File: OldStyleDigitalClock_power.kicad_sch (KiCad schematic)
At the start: 22 parts, among them J1 USB_C_IN, J2 USB_A_OUT, J3 USB_A_OUT, U14 NA555P

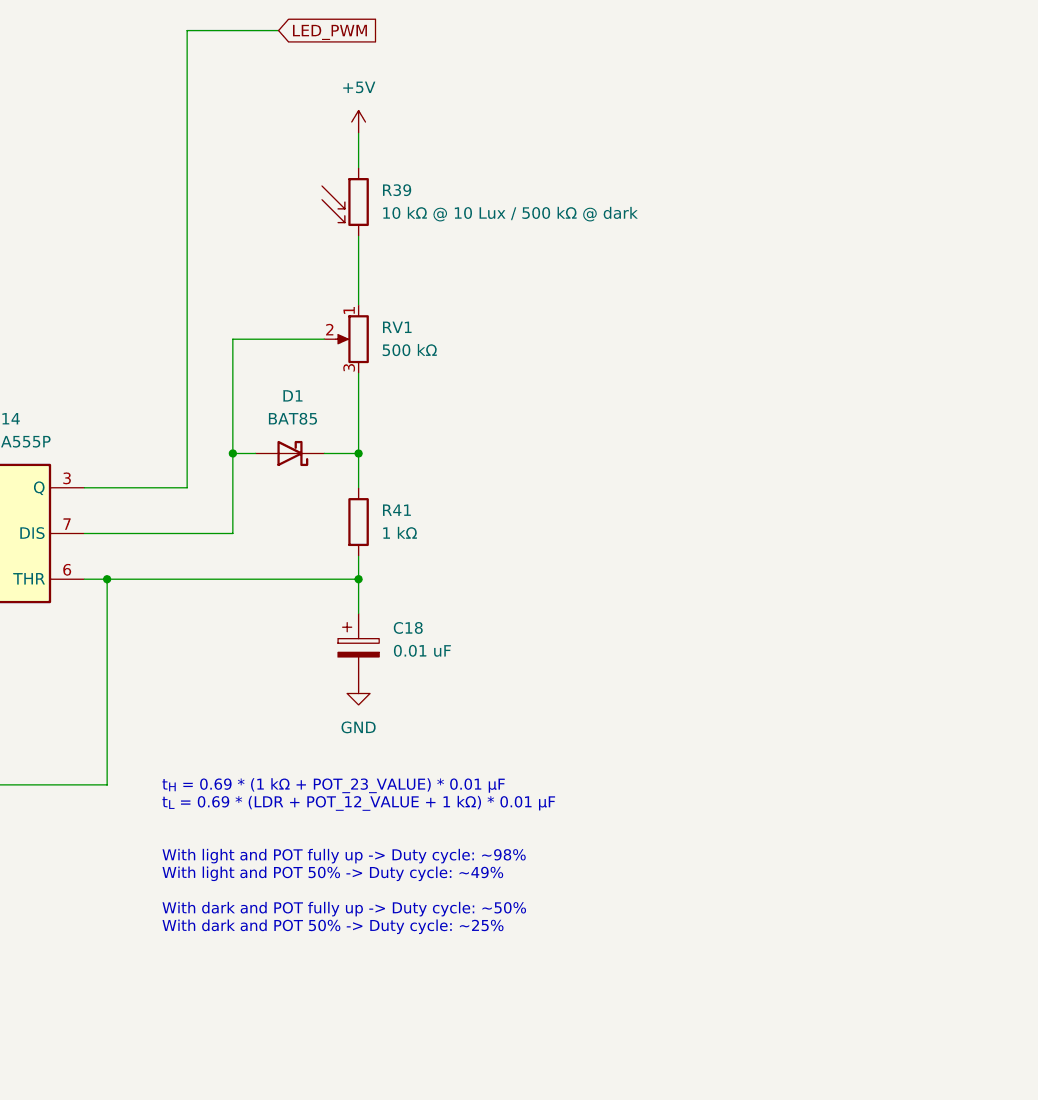
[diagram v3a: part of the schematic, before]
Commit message: Updated PWM calculations
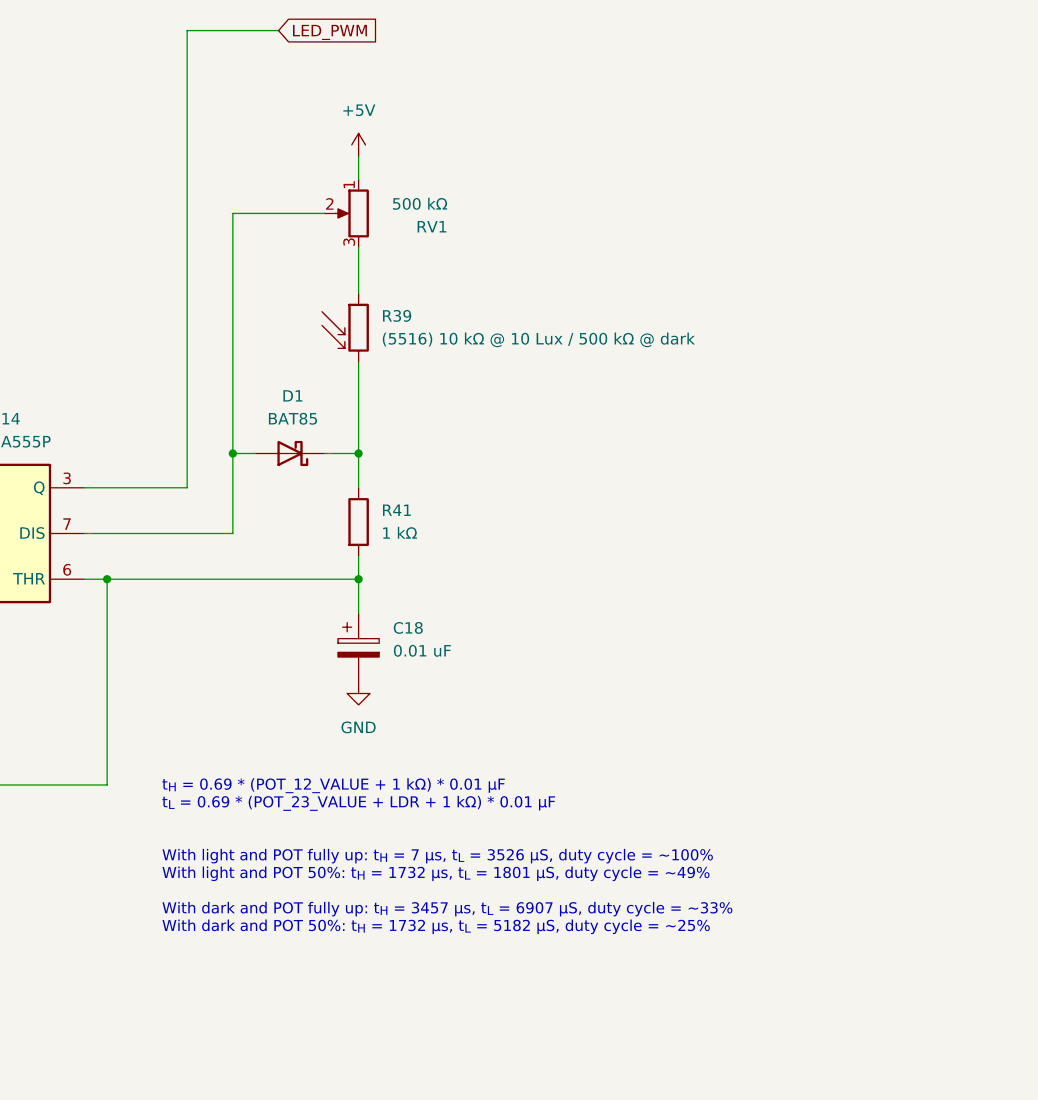
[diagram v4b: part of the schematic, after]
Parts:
- R39: value 10 kΩ @ 10 Lux / 500 kΩ @ dark -> (5516) 10 kΩ @ 10 Lux / 500 kΩ @ dark
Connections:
- net +5V: now also RV1.1; no longer R39.1
- net at R39.2: now also D1.1 (K), R41.1; no longer RV1.1
- new net: R39.1, RV1.3
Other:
- note added: "t_{H} = 0.69 * (POT_12_VALUE + 1 kΩ) * 0.01 µF t_{L} = 0.69 * (POT_23_VALUE + LDR + 1 kΩ) * 0.01 µF With light and POT fully up: t_{H} = 7 µs, t_{L} = 3526 µS, duty cycle = ~100% With light and POT 50%: t_{H} = 1732 µs, t_{L} = 1801 µS, duty cycle = ~49% With dark and POT fully up: t_{H} = 3457 µs, t_{L} = 6907 µS, duty cycle = ~33% With dark and POT 50%: t_{H} = 1732 µs, t_{L} = 5182 µS, duty cy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"
- note removed: "t_{H} = 0.69 * (1 kΩ + POT_23_VALUE) * 0.01 µF t_{L} = 0.69 * (LDR + POT_12_VALUE + 1 kΩ) * 0.01 µF With light and POT fully up -> Duty cycle: ~98% With light and POT 50% -> Duty cycle: ~49% With dark and POT fully up -> Duty cycle: ~50% With dark and POT 50% -> Duty cycle: ~25%"
- moved on the sheet: R39, RV1
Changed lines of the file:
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@@
 		(company "Pasquale Lafiosca")
 	)
-	(text "t_{H} = 0.69 * (1 kΩ + POT_23_VALUE) * 0.01 µF\nt_{L} = 0.69 * (LDR + POT_12_VALUE + 1 kΩ) * 0.01 µF\n\n\nWith light and POT fully up -> Duty cycle: ~98%\nWith light and POT 50% -> Duty cycle: ~49%\n\nWith dark and POT fully up -> Duty cycle: ~50%\nWith dark and POT 50% -> Duty cycle: ~25%"
+	(text "t_{H} = 0.69 * (POT_12_VALUE + 1 kΩ) * 0.01 µF\nt_{L} = 0.69 * (POT_23_VALUE + LDR + 1 kΩ) * 0.01 µF\n\n\nWith light and POT fully up: t_{H} = 7 µs, t_{L} = 3526 µS, duty cycle = ~100%\nWith light and POT 50%: t_{H} = 1732 µs, t_{L} = 1801 µS, duty cycle = ~49%\n\nWith dark and POT fully up: t_{H} = 3457 µs, t_{L} = 6907 µS, duty cycle = ~33%\nWith dark and POT 50%: t_{H} = 1732 µs, t_{L} = 5182 µS, duty cycle = ~25%"
 		(exclude_from_sim no)
 		(at 211.836 111.252 0)
@@
 	)
 	(junction
+		(at 233.68 74.93)
+		(diameter 0)
+		(color 0 0 0 0)
+	)
+	(junction
 		(at 38.1 185.42)
 		(diameter 0)
@@
 	)
 	(junction
-		(at 233.68 74.93)
-		(diameter 0)
-		(color 0 0 0 0)
-	)
-	(junction
 		(at 167.64 67.31)
 		(diameter 0)
@@
 	(wire
 		(pts
+			(xy 219.71 48.26) (xy 219.71 74.93)
+		)
+		(stroke
+			(width 0)
+			(type default)
+		)
+	)
+	(wire
+		(pts
 			(xy 40.64 35.56) (xy 41.91 35.56)
 		)
@@
 	(wire
 		(pts
-			(xy 233.68 39.37) (xy 233.68 43.18)
-		)
-		(stroke
-			(width 0)
-			(type default)
-		)
-	)
-	(wire
-		(pts
 			(xy 88.9 69.85) (xy 88.9 80.01)
 		)
@@
 	(wire
 		(pts
+			(xy 233.68 64.77) (xy 233.68 74.93)
+		)
+		(stroke
+			(width 0)
+			(type default)
+		)
+	)
+	(wire
+		(pts
 			(xy 133.35 90.17) (xy 124.46 90.17)
 		)
@@
 	(wire
 		(pts
-			(xy 219.71 62.23) (xy 229.87 62.23)
-		)
-		(stroke
-			(width 0)
-			(type default)
-		)
-	)
-	(wire
-		(pts
 			(xy 68.58 109.22) (xy 78.74 109.22)
 		)
@@
 	(wire
 		(pts
+			(xy 233.68 41.91) (xy 233.68 44.45)
+		)
+		(stroke
+			(width 0)
+			(type default)
+		)
+	)
+	(wire
+		(pts
 			(xy 68.58 109.22) (xy 68.58 110.49)
 		)
@@
 	(wire
 		(pts
-			(xy 219.71 62.23) (xy 219.71 74.93)
-		)
-		(stroke
-			(width 0)
-			(type default)
-		)
-	)
-	(wire
-		(pts
 			(xy 54.61 69.85) (xy 71.12 69.85)
 		)
@@
 	(wire
 		(pts
-			(xy 233.68 66.04) (xy 233.68 74.93)
+			(xy 233.68 52.07) (xy 233.68 57.15)
 		)
 		(stroke
@@
 	(wire
 		(pts
-			(xy 233.68 50.8) (xy 233.68 58.42)
-		)
-		(stroke
-			(width 0)
-			(type default)
-		)
-	)
-	(wire
-		(pts
 			(xy 31.75 107.95) (xy 31.75 109.22)
 		)
@@
 		(pts
 			(xy 233.68 88.9) (xy 233.68 86.36)
+		)
+		(stroke
+			(width 0)
+			(type default)
+		)
+	)
+	(wire
+		(pts
+			(xy 219.71 48.26) (xy 229.87 48.26)
 		)
 		(stroke
@@
 	(symbol
 		(lib_id "Device:R_Potentiometer")
-		(at 233.68 62.23 0)
+		(at 233.68 48.26 0)
 		(mirror y)
 		(unit 1)
@@
 		(dnp no)
 		(property "Reference" "RV1"
-			(at 236.22 60.9599 0)
-			(effects
-				(font
-					(size 1.27 1.27)
-				)
-				(justify right)
+			(at 243.586 49.784 0)
+			(effects
+				(font
+					(size 1.27 1.27)
+				)
+				(justify left)
 			)
 		)
 		(property "Value" "500 kΩ"
-			(at 236.22 63.4999 0)
-			(effects
-				(font
-					(size 1.27 1.27)
-				)
-				(justify right)
+			(at 243.586 47.244 0)
+			(effects
+				(font
+					(size 1.27 1.27)
+				)
+				(justify left)
 			)
 		)
 		(property "Footprint" ""
-			(at 233.68 62.23 0)
+			(at 233.68 48.26 0)
 			(effects
 				(font
@@
 		)
 		(property "Datasheet" "~"
-			(at 233.68 62.23 0)
+			(at 233.68 48.26 0)
 			(effects
 				(font
@@
 		)
 		(property "Description" "Potentiometer"
-			(at 233.68 62.23 0)
+			(at 233.68 48.26 0)
 			(effects
 				(font
@@
 	(symbol
 		(lib_id "power:VDD")
-		(at 233.68 39.37 0)
+		(at 233.68 41.91 0)
 		(unit 1)
 		(exclude_from_sim no)
@@
 		(dnp no)
 		(property "Reference" "#PWR063"
-			(at 233.68 43.18 0)
+			(at 233.68 45.72 0)
 			(effects
 				(font
@@
 		)
 		(property "Value" "+5V"
-			(at 233.68 34.29 0)
+			(at 233.68 36.83 0)
 			(effects
 				(font
@@
 		)
 		(property "Footprint" ""
-			(at 233.68 39.37 0)
+			(at 233.68 41.91 0)
 			(effects
 				(font
@@
 		)
 		(property "Datasheet" ""
-			(at 233.68 39.37 0)
+			(at 233.68 41.91 0)
 			(effects
 				(font
@@
 		)
 		(property "Description" ""
-			(at 233.68 39.37 0)
+			(at 233.68 41.91 0)
 			(effects
 				(font
@@
 	(symbol
 		(lib_id "Device:R_Photo")
-		(at 233.68 46.99 0)
+		(at 233.68 60.96 0)
 		(unit 1)
 		(exclude_from_sim no)
@@
 		(fields_autoplaced yes)
 		(property "Reference" "R39"
-			(at 236.22 45.7199 0)
-			(effects
-				(font
-					(size 1.27 1.27)
-				)
-				(justify left)
-			)
-		)
-		(property "Value" "10 kΩ @ 10 Lux / 500 kΩ @ dark"
-			(at 236.22 48.2599 0)
+			(at 236.22 59.6899 0)
+			(effects
+				(font
+					(size 1.27 1.27)
+				)
+				(justify left)
+			)
+		)
+		(property "Value" "(5516) 10 kΩ @ 10 Lux / 500 kΩ @ dark"
+			(at 236.22 62.2299 0)
 			(effects
 				(font
@@
 		)
 		(property "Footprint" ""
-			(at 234.95 53.34 90)
+			(at 234.95 67.31 90)
 			(effects
 				(font
@@
 		)
 		(property "Datasheet" "~"
-			(at 233.68 48.26 0)
+			(at 233.68 62.23 0)
 			(effects
 				(font
@@
 		)
 		(property "Description" "Photoresistor"
-			(at 233.68 46.99 0)
-			(effects
-				(font
+			(at 233.68 60.96 0)
+			(effects
+				(font
